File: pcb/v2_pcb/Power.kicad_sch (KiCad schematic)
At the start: 80 parts, among them Q3 NMOS, Q4 NMOS, Q5 NMOS, U10 TPSM863253RDXR, U6 BQ25798RQMR, U7 MAX17320G22+, U8 RPL-3.0-R, U9 RPL-3.0-R

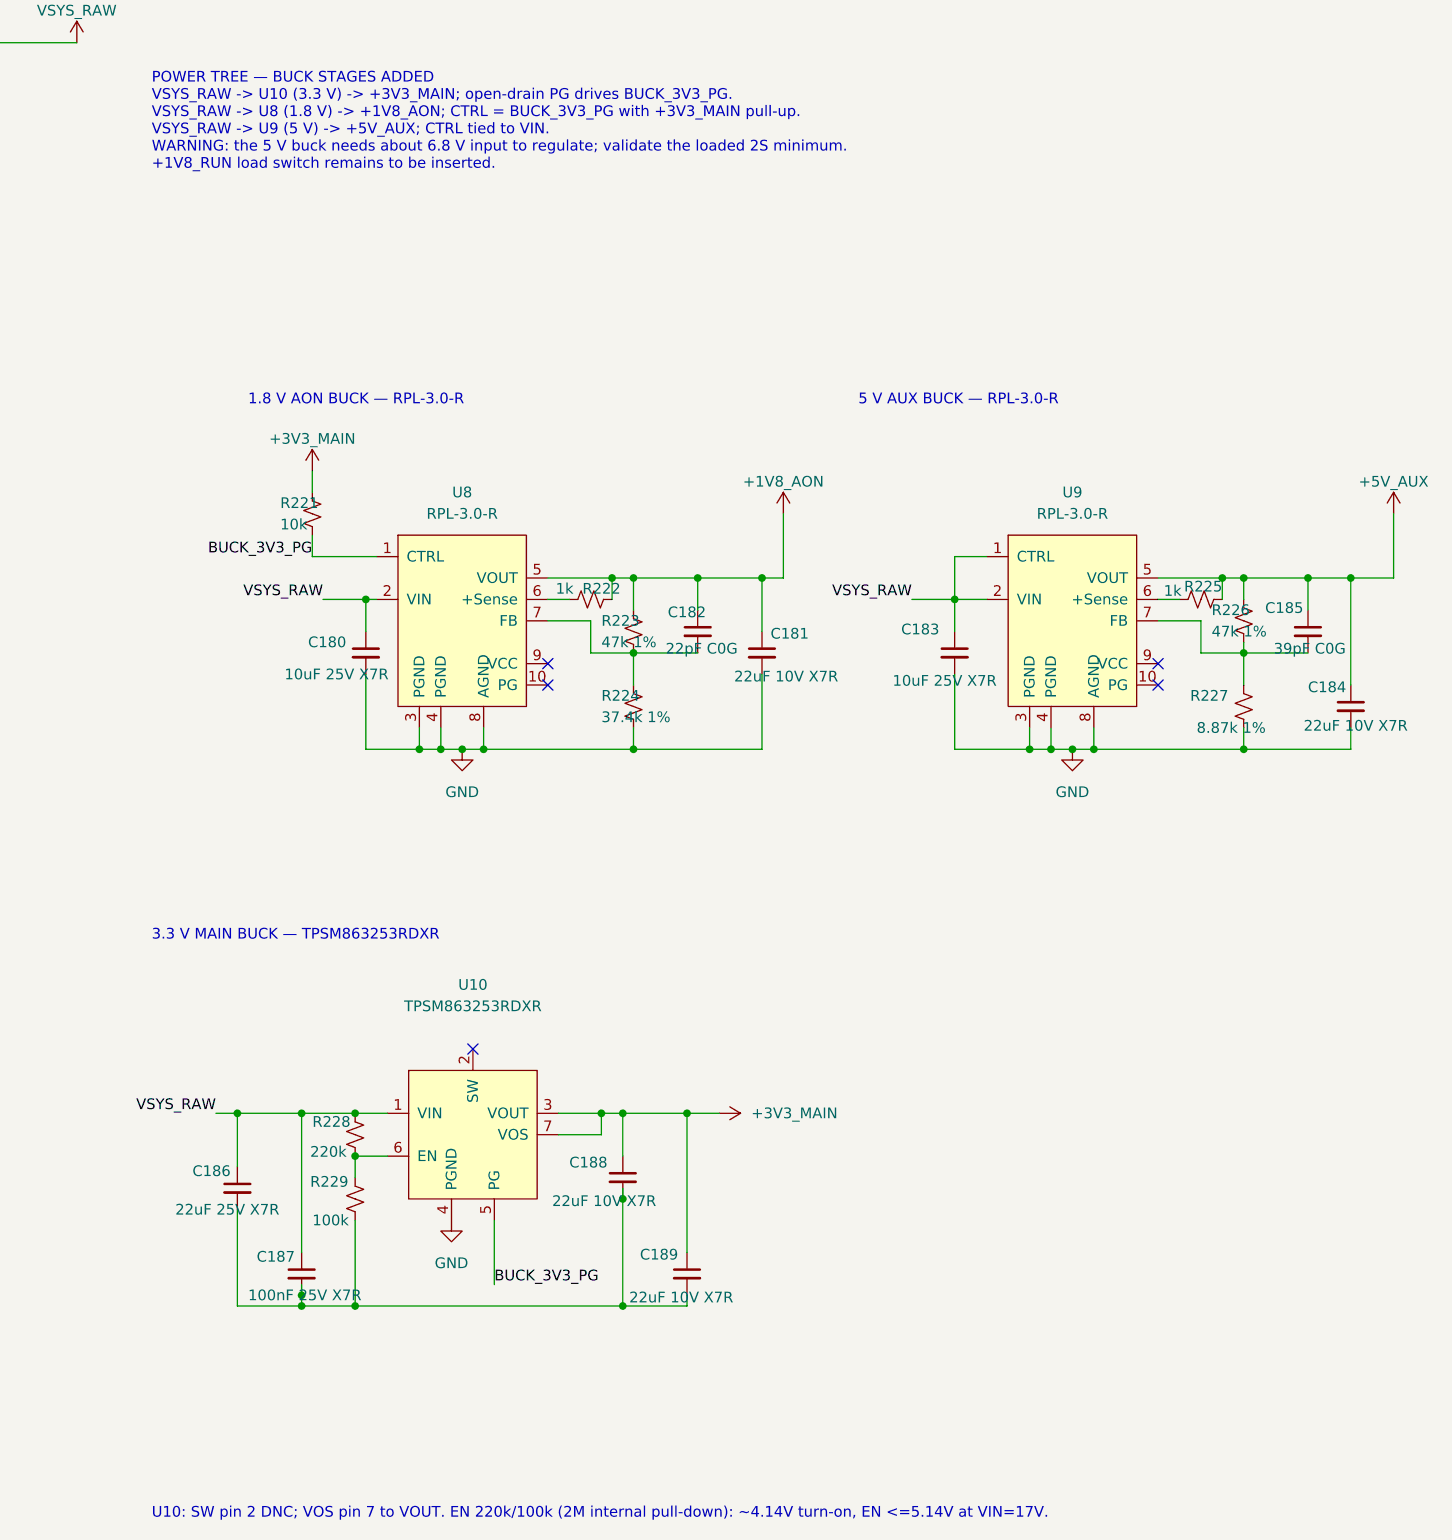
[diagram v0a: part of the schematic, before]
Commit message: run load switch
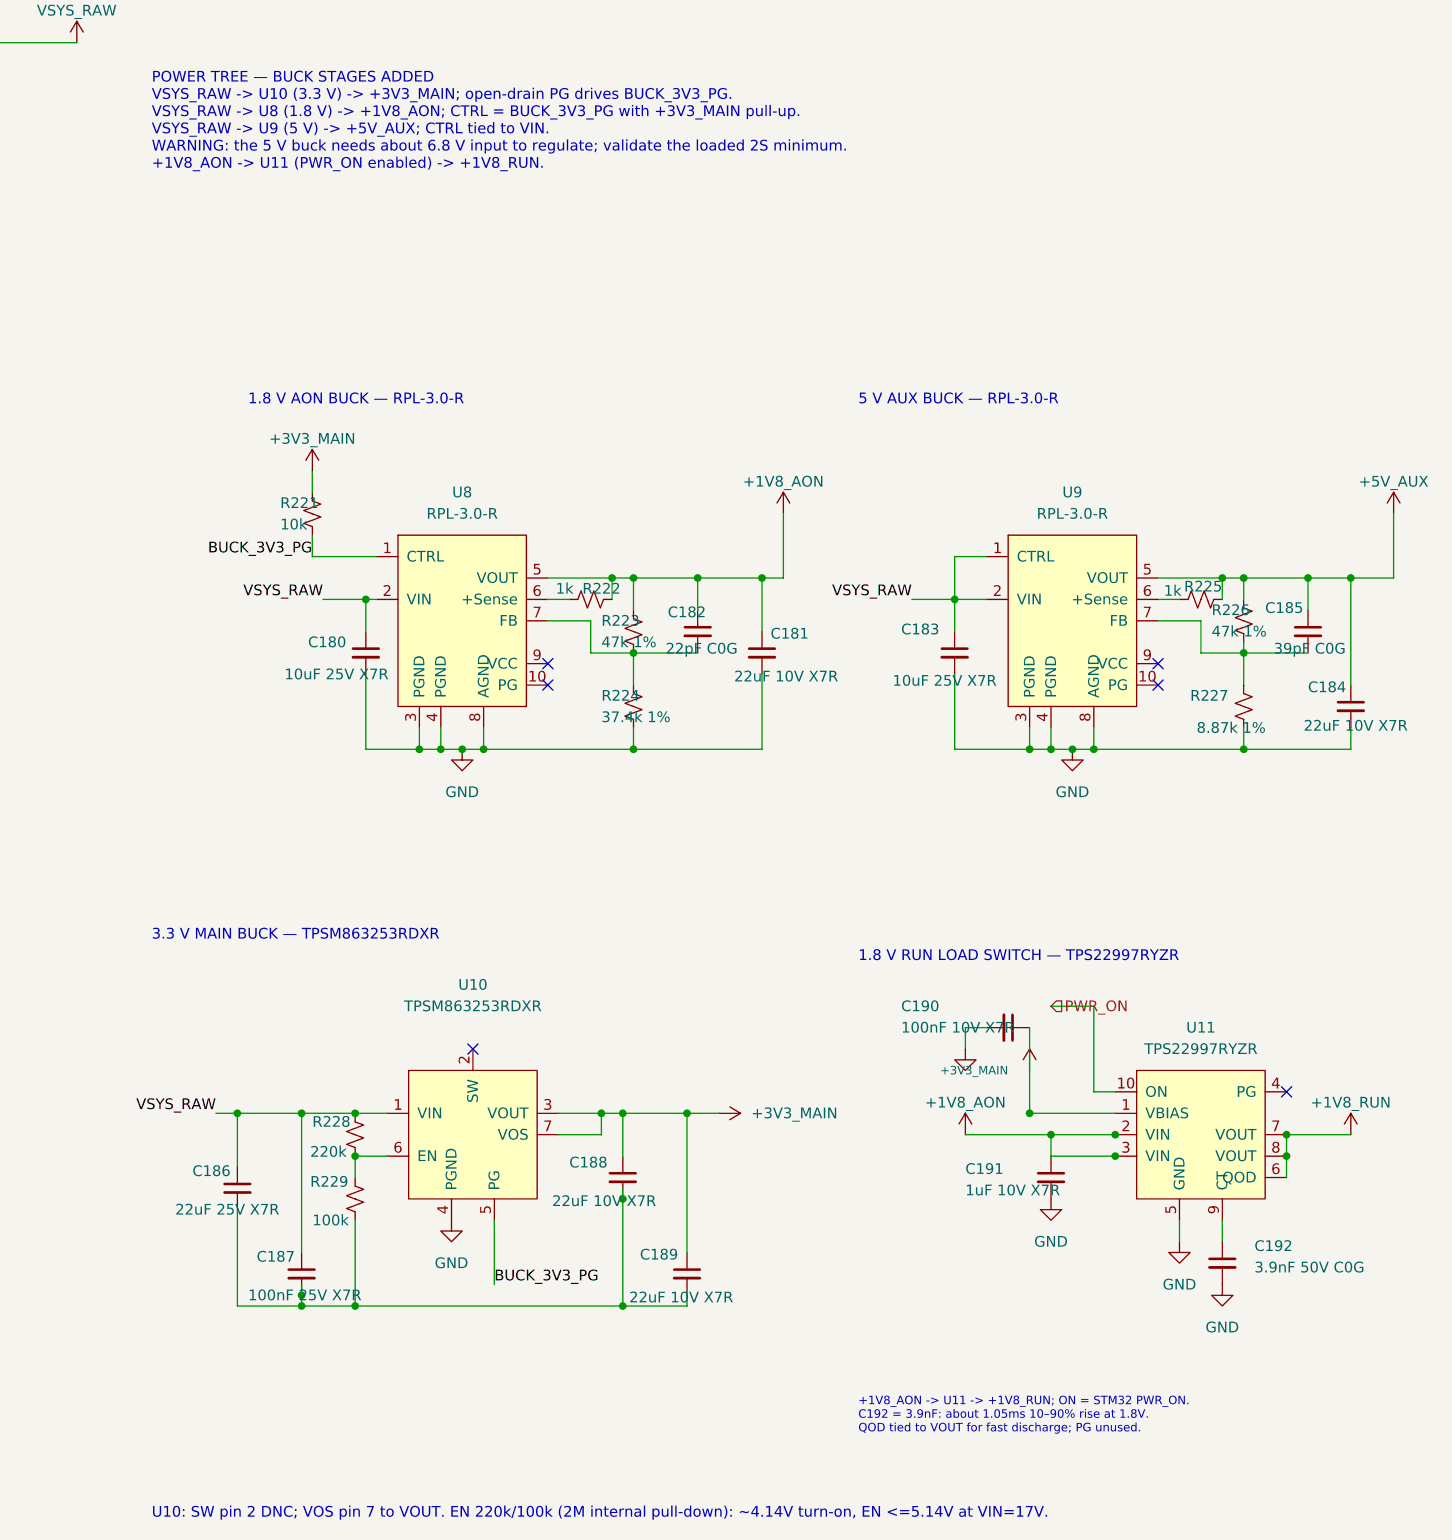
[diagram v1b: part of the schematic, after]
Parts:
- added C190: 100nF 10V X7R, Capacitor_SMD:C_0603_1608Metric, symbol Device:C_Small
- added C191: 1uF 10V X7R, Capacitor_SMD:C_0603_1608Metric, symbol Device:C_Small
- added C192: 3.9nF 50V C0G, Capacitor_SMD:C_0603_1608Metric, symbol Device:C_Small
- added U11: TPS22997RYZR, noob:Texas_RYZ0010A_WQFN-HR-10_2x1.5mm_P0.5mm, symbol open-race:TPS22997RYZR
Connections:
- net +1V8_AON: now also C191.1, U11.2 (VIN), U11.3 (VIN)
- net +3V3_MAIN: now also C190.1, U11.1 (VBIAS)
- net GND: now also C190.2, C191.2, C192.2, U11.5 (GND)
- new net: C192.1, U11.9 (CT)
- new net +1V8_RUN: U11.6 (QOD), U11.7 (VOUT), U11.8 (VOUT)
- new net PWR_ON: U11.10 (ON)
- no-connect marks 7 -> 8
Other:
- note added: "+1V8_AON -> U11 -> +1V8_RUN; ON = STM32 PWR_ON. C192 = 3.9nF: about 1.05ms 10–90% rise at 1.8V. QOD tied to VOUT for fast discharge; PG unused."
- note added: "1.8 V RUN LOAD SWITCH — TPS22997RYZR"
- note added: "POWER TREE — BUCK STAGES ADDED VSYS_RAW -> U10 (3.3 V) -> +3V3_MAIN; open-drain PG drives BUCK_3V3_PG. VSYS_RAW -> U8 (1.8 V) -> +1V8_AON; CTRL = BUCK_3V3_PG with +3V3_MAIN pull-up. VSYS_RAW -> U9 (5 V) -> +5V_AUX; CTRL tied to VIN. WARNING: the 5 V buck needs about 6.8 V input to regulate; validate the loaded 2S minimum. +1V8_AON -> U11 (PWR_ON enabled) -> +1V8_RUN."
- note removed: "POWER TREE — BUCK STAGES ADDED VSYS_RAW -> U10 (3.3 V) -> +3V3_MAIN; open-drain PG drives BUCK_3V3_PG. VSYS_RAW -> U8 (1.8 V) -> +1V8_AON; CTRL = BUCK_3V3_PG with +3V3_MAIN pull-up. VSYS_RAW -> U9 (5 V) -> +5V_AUX; CTRL tied to VIN. WARNING: the 5 V buck needs about 6.8 V input to regulate; validate the loaded 2S minimum. +1V8_RUN load switch remains to be inserted."

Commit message: pcb done
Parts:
- removed BT1, BT2: Battery_Cell, symbol Device:Battery_Cell
- removed C183: 10uF 25V X7R, Capacitor_SMD:C_1206_3216Metric, symbol Device:C_Small
- removed C184: 22uF 10V X7R, Capacitor_SMD:C_1206_3216Metric, symbol Device:C_Small
- removed C185: 39pF C0G, Capacitor_SMD:C_0603_1608Metric, symbol Device:C_Small
- removed Q3, Q4, Q5: NMOS, symbol Simulation_SPICE:NMOS
- removed R225: 1k, Resistor_SMD:R_0603_1608Metric, symbol Device:R_Small_US
- removed R226: 47k 1%, Resistor_SMD:R_0603_1608Metric, symbol Device:R_Small_US
- removed R227: 8.87k 1%, Resistor_SMD:R_0603_1608Metric, symbol Device:R_Small_US
- removed U9: RPL-3.0-R, symbol open-race:RPL-3.0-R
- added C233, C234: 10uF 25V X7R, Capacitor_SMD:C_1210_3225Metric, symbol Device:C_Small
- added C235: 100nF 25V X7R, Capacitor_SMD:C_0603_1608Metric, symbol Device:C_Small
- added C236, C237, C238: 22uF 10V X7R, Capacitor_SMD:C_1210_3225Metric, symbol Device:C_Small
- added C239, C240: 100nF 10V X7R, Capacitor_SMD:C_0603_1608Metric, symbol Device:C_Small
- added C241, C242, C243: 1nF C0G, Capacitor_SMD:C_0603_1608Metric, symbol Device:C_Small
- added C244: 1uF 10V X7R, Capacitor_SMD:C_0603_1608Metric, symbol Device:C_Small
- added C245, C248: 10uF 10V X7R, Capacitor_SMD:C_0805_2012Metric, symbol Device:C_Small
- added C246, C249, C252: 100nF, Capacitor_SMD:C_0603_1608Metric, symbol Device:C_Small
- added C247, C250: 1uF 10V X7R, Capacitor_SMD:C_0805_2012Metric, symbol Device:C_Small
- added C251: 4.7uF 10V X7R, Capacitor_SMD:C_0805_2012Metric, symbol Device:C_Small
- added C255: 2.2uF 35V X7R, Capacitor_SMD:C_1210_3225Metric, symbol Device:C_Small
- added F1: 5A hold / 24V PTC, Fuse:Fuse_2920_7451Metric, symbol Device:Fuse
- added FB20, FB21: 600R@100MHz 1A, Inductor_SMD:L_0805_2012Metric, symbol Device:FerriteBead
- added J20: 2S_PACK_BALANCE, Connector_Molex:Molex_Micro-Fit_3.0_43650-0300_1x03_P3.00mm_Horizontal, symbol Connector_Generic:Conn_01x03
- added L20: 1.5uH XFL4020-152ME, Inductor_SMD:L_Coilcraft_XxL4020, symbol Device:L
- added NTC2: NCP15XH103F03RC 10k B3380, Resistor_SMD:R_0402_1005Metric, symbol Device:Thermistor_NTC_US
- added Q3, Q4, Q5: CSD18540Q5B, open-race-v2:VSON-CLIP-8_DNK_5x6mm, symbol open-race-v2:CSD18540Q5B
- added R240: 10k, Resistor_SMD:R_0603_1608Metric, symbol Device:R_Small_US
- added R244, R245, R246, R247, R248: 100k, Resistor_SMD:R_0603_1608Metric, symbol Device:R_Small_US
- added R252: 2.2R, Resistor_SMD:R_0805_2012Metric, symbol Device:R_Small_US
- added TP20: AUX5_PG, TestPoint:TestPoint_Pad_D1.0mm, symbol Connector:TestPoint_Small
- added U20: TPS630701RNMR (5V fixed), open-race-v2:VQFN-HR-15_RNM_2.5x3mm_P0.5mm, symbol open-race-v2:TPS630701RNMR
- added U21, U22, U23: TPS22918DBVR, open-race-v2:SOT-23-6_DBV, symbol open-race-v2:TPS22918DBVR
- added U26: TVS2200DRVR, Package_SON:WSON-6-1EP_2x2mm_P0.65mm_EP1x1.6mm, symbol Power_Protection:TVS2200DRV
- C10, C42, C56, C62, C81, C82, C84, C85, C87, C88, C9, C91, C93: value 10uF -> 10uF 25V X7R; footprint (none) -> Capacitor_SMD:C_1210_3225Metric
- C11, C13, C14, C7, C83, C86: value 100nF -> 100nF 25V X7R; footprint (none) -> Capacitor_SMD:C_0603_1608Metric
- C12, C8: value 10nF -> 10nF 25V X7R; footprint (none) -> Capacitor_SMD:C_0603_1608Metric
- C15, C16, C17: value 470nF -> 470nF 10V X7R; footprint (none) -> Capacitor_SMD:C_0603_1608Metric
- C49, C53: value 47nF, 10v+ ceram -> 47nF 16V X7R; footprint (none) -> Capacitor_SMD:C_0603_1608Metric
- C92: value 4.7uF -> 4.7uF 10V X7R; footprint (none) -> Capacitor_SMD:C_0805_2012Metric
- D2: value LED -> LTST-C190KGKT GREEN; footprint (none) -> LED_SMD:LED_0603_1608Metric; MPN (none) -> LTST-C190KGKT
- L1: value 2.2uH -> 2.2uH XAL7030-222ME; footprint (none) -> Inductor_SMD:L_Coilcraft_XAL7030-222; MPN (none) -> XAL7030-222ME
- NTC1: footprint (none) -> Resistor_SMD:R_0402_1005Metric; MPN (none) -> NCP15XH103F03RC
- R10, R11, R12, R23, R24, R28, R29, R30, R31, R35, R37, R38, R39, R6, R7, R8, R9: footprint (none) -> Resistor_SMD:R_0603_1608Metric
- R13: value 5m -> 5m 1% 1W; footprint (none) -> Resistor_SMD:R_2512_6332Metric; MPN (none) -> WSL2512R0050FEA
- R25: value 8.2k -> 5.24k 1%; footprint (none) -> Resistor_SMD:R_0603_1608Metric
- R26: value 10k -> 30.3k 1%; footprint (none) -> Resistor_SMD:R_0603_1608Metric
- TP1: footprint (none) -> TestPoint:TestPoint_Pad_D1.0mm
- U7: footprint 21-0139I_T2444-4_MXM -> Package_DFN_QFN:TQFN-24-1EP_4x4mm_P0.5mm_EP2.6x2.6mm; MPN (none) -> MAX17320G22+
- U8: footprint (none) -> open-race-v2:LGA-10_RECOM_RPL-3.0_3x3mm
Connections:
- net CHG_SCL is gone; now on net PMIC_SCL: R30.1, U6.14 (SCL)
- net CHG_SDA is gone; now on net PMIC_SDA: R29.1, U6.15 (SDA)
- net +3V3_MAIN: now also C244.1, R245.1, U21.1 (VIN), U22.1 (VIN), U23.1 (VIN); no longer NTC1.2, U7.10 (TH1)
- net +5V_AUX: now also C236.1, C237.1, C238.1, C239.1, U20.5 (FB), U20.7 (VOUT), U20.8 (VOUT)
- net BAT: now also Q3.1 (S), Q3.2 (S), Q3.3 (S)
- net GND: now also C186.2, C187.2, C188.2, C189.2, R229.2, C233.2, C234.2, C235.2, C236.2, C237.2, C238.2, C239.2, C240.2, C241.2, C242.2, C243.2, C244.2, C245.2, C246.2, C247.2, C248.2, C249.2, C250.2, C251.2, C252.2, C255.2, NTC2.2, R244.2, R246.2, R247.2, R248.2, U20.1 (PS/SYNC), U20.10 (PGND), U20.15 (VSEL), U20.4 (GND), U20.6 (FB2), U21.2 (GND), U22.2 (GND), U23.2 (GND), U26.1 (GND), U26.2 (GND), U26.3 (GND), U26.7 (GND)
- net GND1: now also J20.3 (Pin_3)
- net VSYS_RAW: now also C233.1, C234.1, C235.1, U20.12 (VIN), U20.13 (VIN)
- net vpack+: now also Q3.5 (D), Q3.6 (D), Q3.7 (D), Q3.8 (D), Q5.1 (S), Q5.2 (S), Q5.3 (S), R240.1; no longer U7.5 (ZVC)
- net BQ_SW1: now reaches C49.1, L1.1, U6.28 (SW1)
- net BQ_SW2: now reaches C53.1, L1.2, U6.26 (SW2)
- net MAX_IN_SENSE: now reaches C13.2, C14.1, R10.2, U7.1 (IN)
- net MAX_AOLDO: now reaches C17.1, U7.12 (AOLDO)
- net MAX_REG3: now reaches C15.1, U7.13 (REG3)
- net MAX_REG2: now reaches C16.1, U7.17 (REG2)
- net MAX_CELL1_SENSE: now reaches C12.1, C8.2, R12.2, U7.21 (CELL1)
- net MAX_CELL1_SENSE: no longer U7.22 (CELL2), U7.23 (CELL3)
- net MAX_TOP_SENSE: now reaches C8.1, R11.2, U7.24 (BATTS)
- net MAX_TOP_SENSE: now also U7.22 (CELL2), U7.23 (CELL3)
- net MAX_CHG_BIAS: now reaches R7.2, U7.3 (CHG)
- net MAX_DIS_BIAS: now reaches R8.2, U7.4 (DIS)
- net MAX_PCKP_SENSE: now reaches R6.2, U7.6 (PCKP)
- net BQ_PROG_SET: now reaches R35.2, U6.20 (PROG)
- net VBUS_PD: now reaches C10.2, C11.2, C42.2, C9.2, U6.2 (VBUS), U6.3 (VBUS), U6.8 (VAC2), U6.9 (VAC1)
- net VBUS_PD: now also R252.1, U26.4 (IN), U26.5 (IN), U26.6 (IN)
- net BQ_TS: now reaches R25.2, R26.2, U6.16 (TS)
- net BQ_TS: now also NTC2.1
- net BQ_STAT: now reaches R28.1, U6.1 (STAT)
- net BQ_STAT_LED: now reaches D2.1 (K), R28.2
- net BQ_BATP_SENSE: now reaches R23.1, U6.18 (BATP)
- net MAX_CHG_GATE: now reaches C7.2, R7.1
- net MAX_CHG_GATE: now also Q4.4 (G)
- net PACK_POS: now reaches C7.1, R10.1, R11.1
- net PACK_POS: now also F1.1, Q4.1 (S), Q4.2 (S), Q4.3 (S)
- net MAX_DIS_GATE: now reaches R8.1
- net MAX_DIS_GATE: now also Q5.4 (G)
- net BQ_PMID: now reaches C86.2, C87.2, C88.2, C91.2, U6.29 (PMID)
- net CELL_MID: now reaches R12.1
- net CELL_MID: now also J20.2 (Pin_2)
- net RUN_QOD: now reaches C192.1, U11.9 (CT)
- net BQ_QON_TP: now reaches TP1.1, U6.12 (~{QON})
- net BQ_BTST2: now reaches C53.2, U6.19 (BTST2)
- net BQ_SDRV: now reaches U6.24 (SDRV)
- net BQ_SDRV: now also Q3.4 (G)
- net BQ_BTST1: now reaches C49.2, U6.4 (BTST1)
- net RPL_SENSE: now reaches R222.1, U8.6 (+Sense)
- net RPL_FB: now reaches C182.2, R223.2, R224.1, U8.7 (FB)
- net BUCK_3V3_EN: now reaches R228.2, R229.1, U10.6 (EN)
- net BAT_SCL renamed PMIC_SCL
- net BAT_SDA renamed PMIC_SDA
- new net +3V3_GNSS_CLEAN: C248.1, C249.1, FB20.1
- new net +3V3_IMU_CLEAN: C251.1, C252.1, FB21.1
- new net +3V3_RADIO_SW: C245.1, C246.1, U21.5 (QOD), U21.6 (VOUT)
- new net AUX5_EN: R244.1, U20.14 (EN)
- new net AUX5_PG: R245.2, TP20.1, U20.2 (PG)
- new net AUX_SW1: L20.2, U20.11 (L1)
- new net AUX_SW2: L20.1, U20.9 (L2)
- new net AUX_VAUX: C240.1, U20.3 (VAUX)
- new net GNSS_EN: R247.1, U22.3 (ON)
- new net GNSS_EN_CT: C242.1, U22.4 (CT)
- new net GNSS_SW_RAW: C247.1, FB20.2, U22.5 (QOD), U22.6 (VOUT)
- new net IMU_EN: R248.1, U23.3 (ON)
- new net IMU_EN_CT: C243.1, U23.4 (CT)
- new net IMU_SW_RAW: C250.1, FB21.2, U23.5 (QOD), U23.6 (VOUT)
- new net MAX_FET_COMMON: Q4.5 (D), Q4.6 (D), Q4.7 (D), Q4.8 (D), Q5.5 (D), Q5.6 (D), Q5.7 (D), Q5.8 (D)
- new net MAX_TH1_NTC: NTC1.2, U7.10 (TH1)
- new net MAX_ZVC: R240.2, U7.5 (ZVC)
- new net PACK_POS_CONN: F1.2, J20.1 (Pin_1)
- new net RADIO_EN: R246.1, U21.3 (ON)
- new net RADIO_EN_CT: C241.1, U21.4 (CT)
- new net VBUS_SNUBBER: C255.1, R252.2
- no-connect marks 8 -> 6
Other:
- note added: "3V3 branches: RADIO load-switched; GNSS/IMU load-switched then C-FB-C filtered."
- note added: "5 V AUX: TPS630701 fixed buck-boost; AUX5_EN controls EN; power-save mode selected."
- note added: "COMMISSIONING - BQ25798: RPROG=8.2k selects 2S / 750kHz at POR; charge current remains at the 1A default until firmware raises it only after thermal and cell checks pass."
- note added: "COMMISSIONING - MAX17320 NVM: before enabling charge, program and validate nPackCfg for 2S (NCELLS=0), one 10k TH1, nRSense=5mOhm, and the selected 21700 cell model/capacity/protection limits. Wiring alone does not define these settings."
- note added: "MAX17320 2S: CELL1=cell midpoint; CELL2=CELL3=BATTS=filtered pack top, per datasheet Figure 24 / Note 10."
- note added: "PACK TEMPERATURE: initial build must thermally couple both NTC1 (MAX17320 TH1) and fitted NTC2 (BQ25798 TS) to the pack. Keep BQ TS_IGNORE=0; configure MAX for the NCP15 10k/B3380 model; validate hot/cold thresholds before raising charge current."
- note added: "PMIC_SCL/SDA direct host link is valid across only R13=5mOhm Kelvin shunt; preserve GND1 (cell/CSP) / GND (system/CSN) separation and do not bridge elsewhere."
- note added: "PRE-LAYOUT HOLD: verify Q1-Q5/F1 current, SOA, copper, thermal vias and connector temperature rise at worst-case charge/load current."
- note added: "VBUS HOT-PLUG: TVS2200 clamps VBUS_PD and populated 2.2R/2.2uF snubber damps cable ringing; scope and tune after worst-cable testing. TVS2200 is for SPR <=20V / 21V ceiling only - never enable 28V EPR."

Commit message: switch mosfets
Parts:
- Q3, Q4, Q5: value CSD18540Q5B -> NMOS

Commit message: power and debug cleanup
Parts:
- removed C255: 2.2uF 35V X7R, Capacitor_SMD:C_1210_3225Metric, symbol Device:C_Small
- removed R252: 2.2R, Resistor_SMD:R_0805_2012Metric, symbol Device:R_Small_US
- removed U26: TVS2200DRVR, Package_SON:WSON-6-1EP_2x2mm_P0.65mm_EP1x1.6mm, symbol Power_Protection:TVS2200DRV
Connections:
- net BQ_TS: no longer NTC2.1, R25.2, R26.2, U6.16 (TS)
- net PACK_POS: now also F1.2, J20.1 (Pin_1)
- net PACK_POS_CONN: no longer F1.2, J20.1 (Pin_1)
- net REGN: now also R24.2; no longer R24.1
- net at U6.17 (ILIM_HIZ): now also R24.1; no longer R24.2
- net AUX5_PG: no longer names the net of R245.2, TP20.1, U20.2 (PG)
- net BAT: no longer names the net of C84.1, C85.1, Q3.1 (S), Q3.2 (S), Q3.3 (S), U6.22 (BAT), U6.23 (BAT)
- net BQ_SDRV: no longer names the net of Q3.4 (G), U6.24 (SDRV)
- net MAX_CHG_BIAS: no longer names the net of R7.2, U7.3 (CHG)
- net MAX_CHG_GATE: no longer names the net of C7.2, Q4.4 (G), R7.1
- net MAX_DIS_BIAS: no longer names the net of R8.2, U7.4 (DIS)
- net MAX_DIS_GATE: no longer names the net of Q5.4 (G), R8.1
- net MAX_FET_COMMON: no longer names the net of Q4.5 (D), Q4.6 (D), Q4.7 (D), Q4.8 (D), Q5.5 (D), Q5.6 (D), Q5.7 (D), Q5.8 (D)
- net MAX_PCKP_SENSE: no longer names the net of R6.2, U7.6 (PCKP)
- net MAX_ZVC: no longer names the net of R240.2, U7.5 (ZVC)
- net RADIO_EN_CT: no longer names the net of C241.1, U21.4 (CT)
- new net: NTC2.1, R25.2, R26.2, U6.16 (TS)
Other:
- moved on the sheet: C233, C234, C235, C236, C237, C238, C239, C240, C241, C244, C245, F1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

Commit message: fix minor
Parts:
- C235: value 100nF 25V X7R -> 10uF 25V X5R
- C239: value 100nF 10V X7R -> 10uF 25V X5R
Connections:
- net vpack+: no longer Q5.1 (S), Q5.2 (S), Q5.3 (S)
- net at Q5.4 (G): no longer R8.1
- net at Q5.5 (D), Q5.6 (D), Q5.7 (D)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: no longer Q4.5 (D), Q4.6 (D), Q4.7 (D), Q4.8 (D)
- new net: Q5.1 (S), Q5.2 (S), Q5.3 (S)
- new net: Q4.5 (D), Q4.6 (D), Q4.7 (D), Q4.8 (D)
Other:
- moved on the sheet: Q5
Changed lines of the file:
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@@
 	(symbol
 		(lib_id "open-race-v2:CSD18540Q5B")
-		(at 160.02 154.94 90)
+		(at 160.02 154.94 270)
 		(unit 1)
 		(body_style 1)
@@
 			)
 		)
-		(property "Value" "100nF 10V X7R"
+		(property "Value" "10uF 25V X5R"
 			(at 538.734 114.808 0)
 			(show_name no)
@@
 			)
 		)
-		(property "Value" "100nF 25V X7R"
+		(property "Value" "10uF 25V X5R"
 			(at 468.884 83.058 0)
 			(show_name no)
